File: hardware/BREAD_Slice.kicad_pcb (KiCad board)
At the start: 2 copper layers, 70 x 100 mm, 22 parts, among them J1 Conn_01x10_Socket, SW1 SW_DIP_x04, U1 AP63205

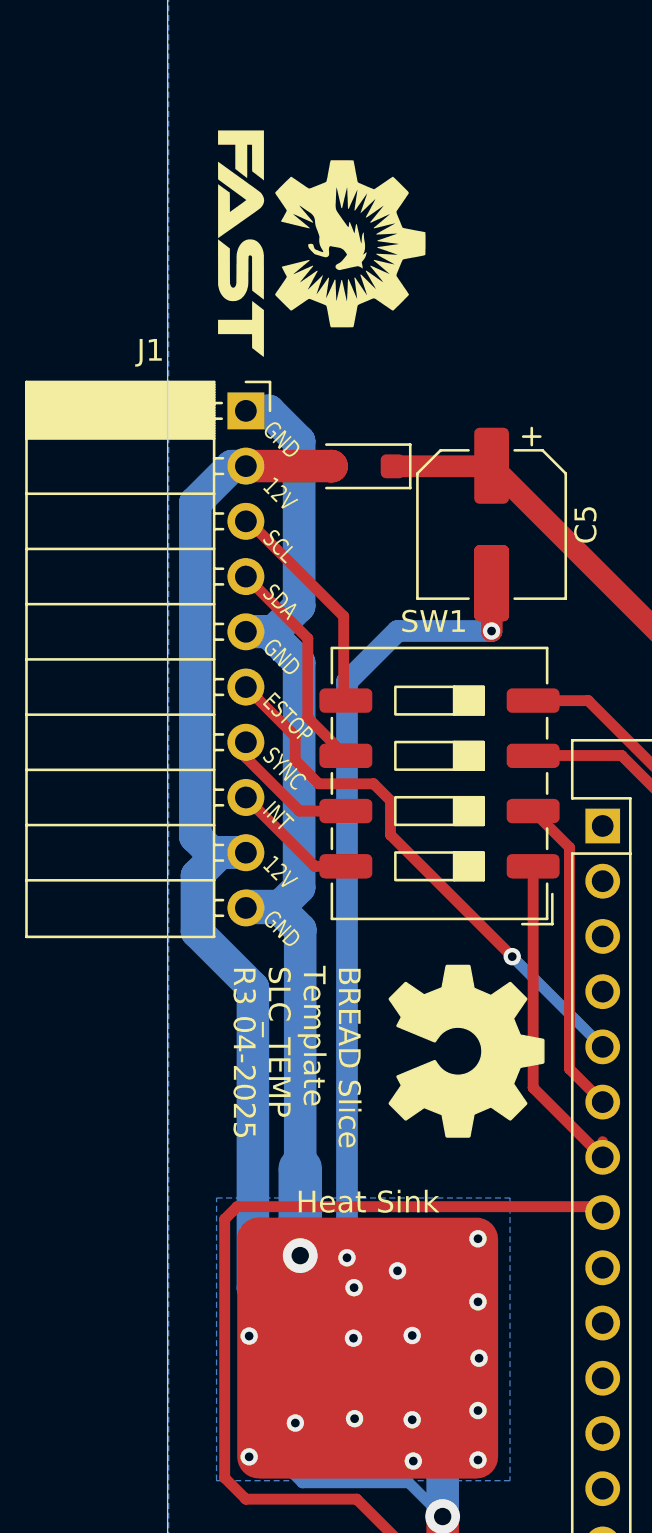
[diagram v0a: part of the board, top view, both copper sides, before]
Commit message: update gitignore
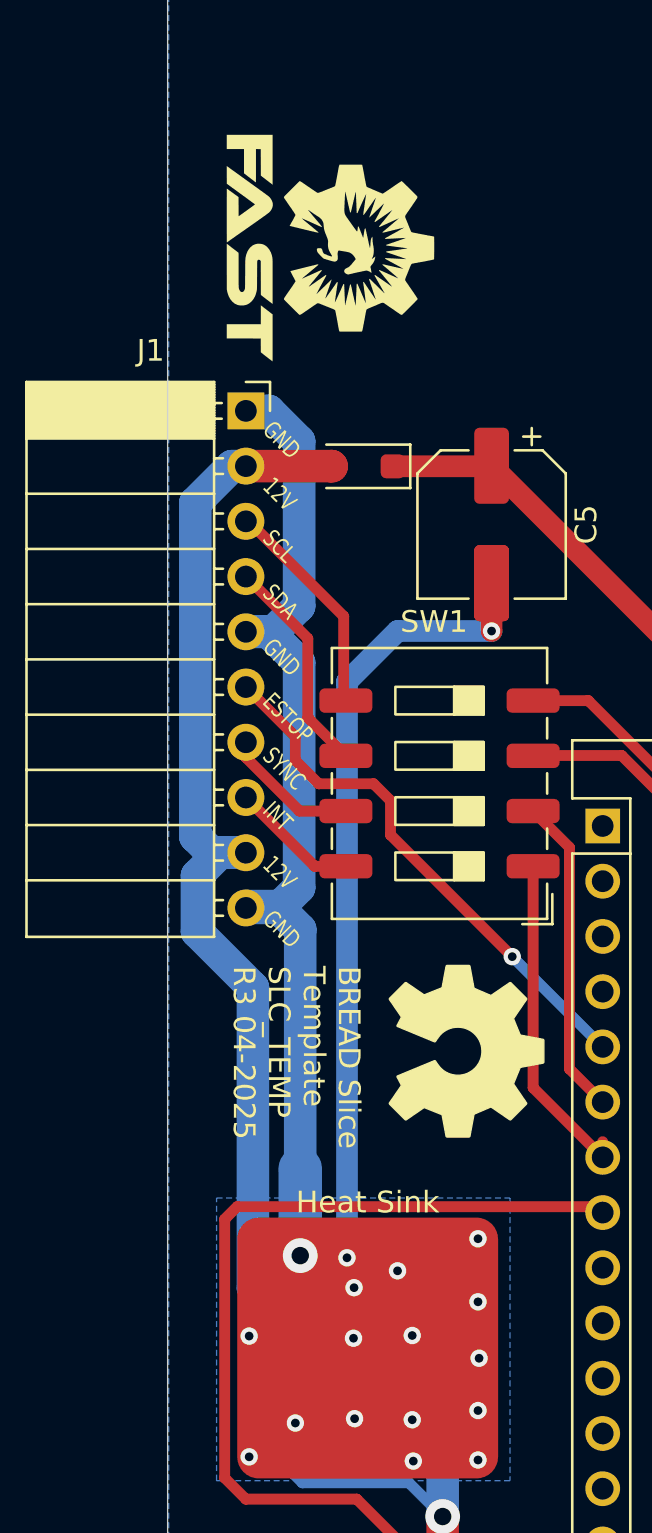
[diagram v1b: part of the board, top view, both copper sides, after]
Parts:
- removed the G*** at (130.1, 70.3)
- added G***: LOGO, KMLib_Aesthetic:FAST-Logo-Medium, F.Cu at (130.5, 70.5)
- A1: footprint kml-custom:Arduino_Nano_Headers -> KMLib_Boards_Modules:Arduino_Nano_Headers
- D2: footprint kml-custom:WS2812-5050-4PIN -> KMLib_IC_SMD:WS2812-5050-4PIN
- HS1: footprint kml-custom:Thermal Pad -> KMLib_Mounting:Thermal Pad
- Ref**: footprint kml-custom:OSHW_Logo_8mm -> KMLib_Aesthetic:OSHW_Logo_8mm
- U1: footprint kml-custom:SOIC_05WU-7_DIO-M -> KMLib_IC_SMD:SOIC_05WU-7_DIO
